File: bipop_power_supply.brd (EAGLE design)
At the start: 82.5 x 70.8 mm, 33 parts, among them IC1 LM1117MP-3.3, IC2 LM1117MP-5.0, X2 MSTBA6

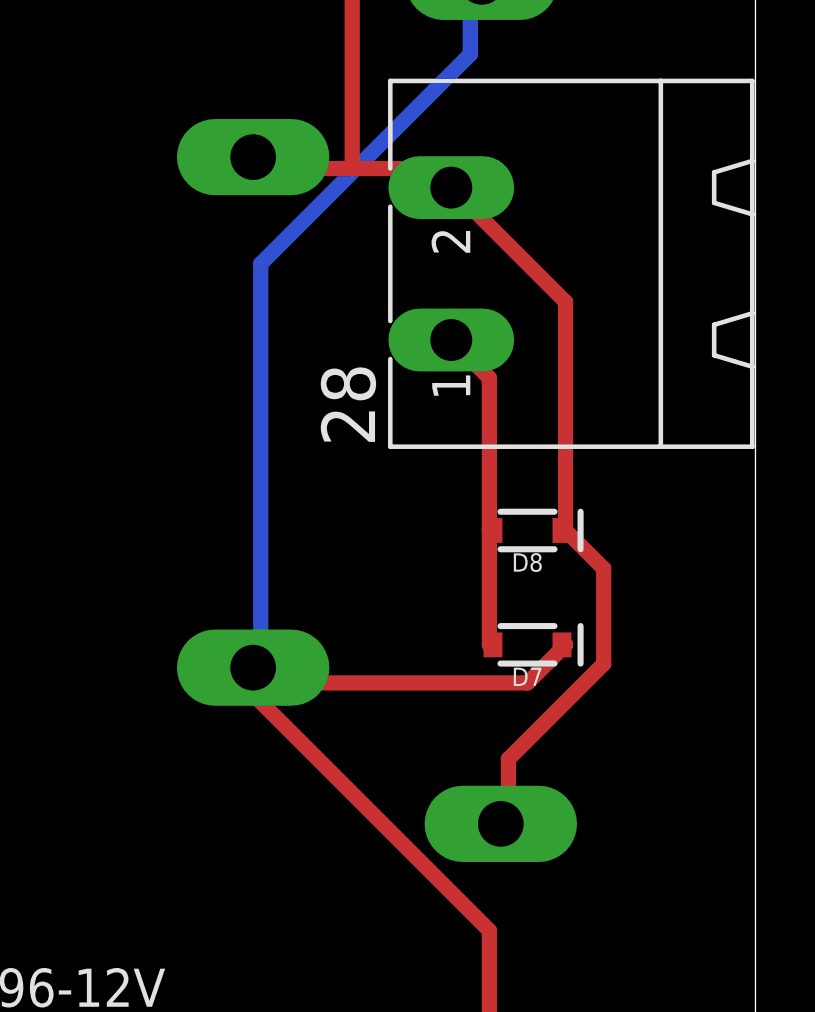
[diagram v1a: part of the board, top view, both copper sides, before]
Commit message: changed diodes' packages
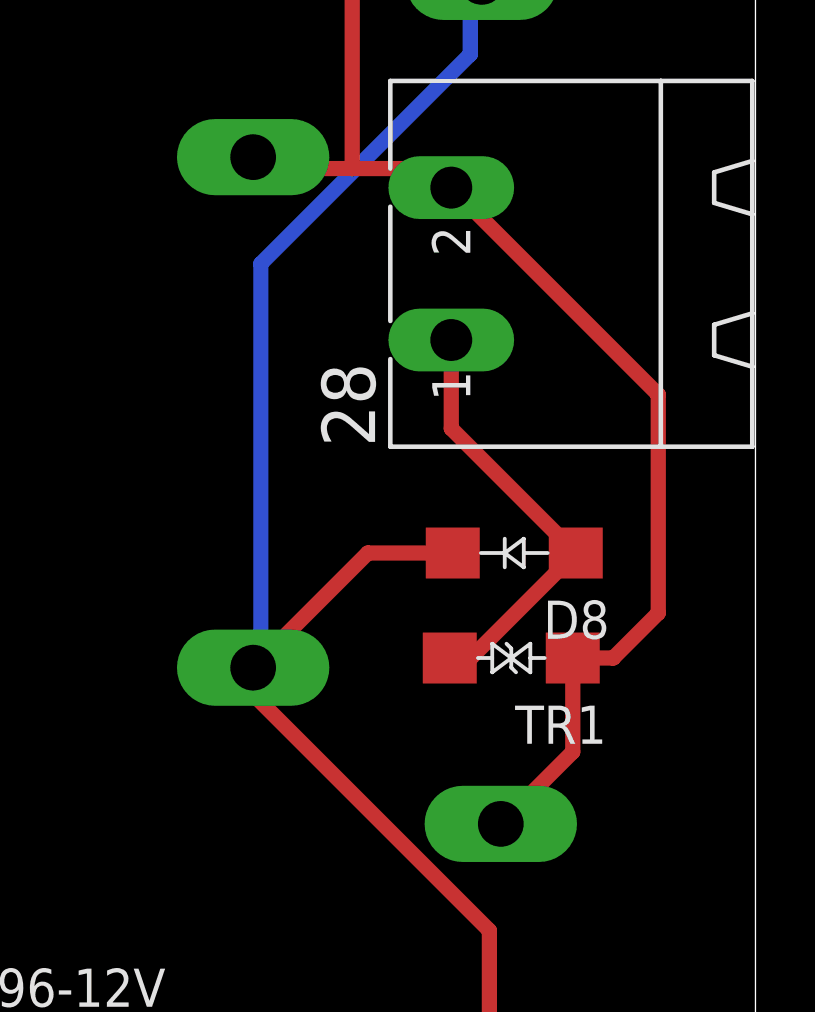
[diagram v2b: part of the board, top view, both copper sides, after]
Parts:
- removed D7: 20V, SparkFun-DiscreteSemi:SOD-323
- added TR1: SMBJ30CA-TR, transil:DO214AC_BIDIR
- D8: value 33.3V -> GF1; device SparkFun-DiscreteSemi:SOD-323 -> _mod_diode:SMA-DO214AC
- moved D8 0.87 mm to (78.3, 31.0)
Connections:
- net MM: now also D8.K; no longer D7.C
- net N$10: now also TR1.P$1; no longer D8.C
- net N$12: now also TR1.P$2; no longer D7.A
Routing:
- net N$12: track 10.9 -> 14.5 mm
- net MM: track 63.5 -> 60.3 mm
- net N$10: track 57.0 -> 59.1 mm
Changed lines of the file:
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@@
 <?xml version="1.0" encoding="utf-8"?>
 <!DOCTYPE eagle SYSTEM "eagle.dtd">
-<eagle version="8.5.1">
+<eagle version="8.3.2">
 <drawing>
 <settings>
@@
 <setting verticaltext="up"/>
 </settings>
-<grid distance="10" unitdist="mil" unit="mil" style="lines" multiple="1" display="yes" altdistance="5" altunitdist="mil" altunit="mil"/>
+<grid distance="0.1" unitdist="mm" unit="mm" style="lines" multiple="1" display="yes" altdistance="5" altunitdist="mil" altunit="mil"/>
 <layers>
 <layer number="1" name="Top" color="4" fill="1" visible="yes" active="yes"/>
@@
 <param name="dpMaxLengthDifference" value="10mm"/>
 <param name="dpGapFactor" value="2.5"/>
+<param name="checkGrid" value="0"/>
 <param name="checkAngle" value="0"/>
 <param name="checkFont" value="1"/>
 <param name="checkRestrict" value="1"/>
-<param name="checkStop" value="0"/>
-<param name="checkValues" value="0"/>
 <param name="useDiameter" value="13"/>
 <param name="maxErrors" value="50"/>
@@
 </element>
 <element name="U$4" library="frames" library_urn="urn:adsk.eagle:library:229" package="A5P-LOC" value="" x="-31.75" y="-48.26"/>
-<element name="D7" library="SparkFun-DiscreteSemi" package="SOD-323" value="20V" x="78.74" y="27.94" rot="R180">
-<attribute name="PROD_ID" value="DIO-11284" x="78.74" y="27.94" size="1.778" layer="27" rot="R180" display="off"/>
-</element>
 <element name="C1" library="rcl" library_urn="urn:adsk.eagle:library:334" package="C0805" package3d_urn="urn:adsk.eagle:package:23617/2" value="100uF" x="25.146" y="34.29" rot="R90"/>
-<element name="D8" library="SparkFun-DiscreteSemi" package="SOD-323" value="33.3V" x="78.74" y="31.75" rot="R180">
-<attribute name="PROD_ID" value="DIO-11284" x="78.74" y="31.75" size="1.778" layer="27" rot="R180" display="off"/>
-</element>
 <element name="C2" library="rcl" library_urn="urn:adsk.eagle:library:334" package="C0805" package3d_urn="urn:adsk.eagle:package:23617/2" value="100uF" x="25.146" y="40.64" rot="R90"/>
 <element name="C3" library="rcl" library_urn="urn:adsk.eagle:library:334" package="C0805" package3d_urn="urn:adsk.eagle:package:23617/2" value="100uF" x="25.146" y="46.736" rot="R90"/>
@@
 <element name="R2" library="rcl" library_urn="urn:adsk.eagle:library:334" package="R0805" package3d_urn="urn:adsk.eagle:package:23553/2" value="4.7k" x="12.573" y="9.525" rot="R270"/>
 <element name="R3" library="rcl" library_urn="urn:adsk.eagle:library:334" package="R0805" package3d_urn="urn:adsk.eagle:package:23553/2" value="4.7k" x="6.985" y="26.035" rot="R270"/>
+<element name="TR1" library="transil" package="DO214AC_BIDIR" value="SMBJ30CA-TR" x="78.2" y="27.5" rot="R180"/>
+<element name="D8" library="_mod_diode" package="SMA-DO214AC" value="GF1" x="78.3" y="31" rot="R180"/>
 </elements>
 <signals>
@@
 </signal>
 <signal name="N$10">
-<contactref element="D8" pad="C"/>
 <contactref element="U$1" pad="V_IN-"/>
 <contactref element="U$2" pad="V_IN-"/>
 <contactref element="U$3" pad="V_IN-"/>
 <contactref element="28" pad="2"/>
-<wire x1="80.01" y1="39.37" x2="80.01" y2="31.75" width="0.508" layer="1"/>
-<wire x1="76.2" y1="43.18" x2="80.01" y2="39.37" width="0.508" layer="1"/>
-<wire x1="78.105" y1="24.13" x2="78.105" y2="22.225" width="0.508" layer="1"/>
-<wire x1="81.28" y1="27.305" x2="78.105" y2="24.13" width="0.508" layer="1"/>
-<wire x1="81.28" y1="30.48" x2="81.28" y2="27.305" width="0.508" layer="1"/>
-<wire x1="80.01" y1="31.75" x2="81.28" y2="30.48" width="0.508" layer="1"/>
-<wire x1="78.105" y1="22.225" x2="77.851" y2="21.971" width="0.508" layer="1"/>
-<wire x1="80.01" y1="31.75" x2="79.89" y2="31.75" width="0.508" layer="1"/>
 <wire x1="75.565" y1="43.815" x2="72.898" y2="43.815" width="0.508" layer="1"/>
 <wire x1="72.898" y1="43.815" x2="69.85" y2="43.815" width="0.508" layer="1"/>
@@
 <wire x1="72.898" y1="43.815" x2="72.898" y2="53.086" width="0.508" layer="1"/>
 <wire x1="76.835" y1="66.675" x2="77.216" y2="67.056" width="0.508" layer="1"/>
+<contactref element="TR1" pad="P$1"/>
+<wire x1="77.851" y1="21.971" x2="80.25" y2="24.37" width="0.508" layer="1"/>
+<wire x1="80.25" y1="24.37" x2="80.25" y2="27.5" width="0.508" layer="1"/>
+<wire x1="80.25" y1="27.5" x2="81.6" y2="27.5" width="0.508" layer="1"/>
+<wire x1="81.6" y1="27.5" x2="83.1" y2="29" width="0.508" layer="1"/>
+<wire x1="83.1" y1="29" x2="83.1" y2="36.28" width="0.508" layer="1"/>
+<wire x1="83.1" y1="36.28" x2="76.2" y2="43.18" width="0.508" layer="1"/>
 </signal>
 <signal name="N$12">
+<contactref element="28" pad="1"/>
+<contactref element="TR1" pad="P$2"/>
 <contactref element="D8" pad="A"/>
-<contactref element="D7" pad="A"/>
-<contactref element="28" pad="1"/>
-<wire x1="77.47" y1="31.75" x2="77.47" y2="27.94" width="0.508" layer="1"/>
-<wire x1="77.47" y1="27.94" x2="77.59" y2="27.94" width="0.508" layer="1"/>
-<wire x1="77.47" y1="36.83" x2="77.47" y2="31.75" width="0.508" layer="1"/>
-<wire x1="76.2" y1="38.1" x2="77.47" y2="36.83" width="0.508" layer="1"/>
-<wire x1="77.47" y1="31.75" x2="77.59" y2="31.75" width="0.508" layer="1"/>
+<wire x1="76.85" y1="27.5" x2="80.35" y2="31" width="0.508" layer="1"/>
+<wire x1="76.85" y1="27.5" x2="76.15" y2="27.5" width="0.508" layer="1"/>
+<wire x1="80.35" y1="31" x2="76.2" y2="35.15" width="0.508" layer="1"/>
+<wire x1="76.2" y1="35.15" x2="76.2" y2="38.1" width="0.508" layer="1"/>
 </signal>
 <signal name="VIOUT_5">
@@
 <signal name="MM">
 <contactref element="U$1" pad="V_IN+"/>
-<contactref element="D7" pad="C"/>
 <contactref element="U$2" pad="V_IN+"/>
 <contactref element="U$3" pad="V_IN+"/>
-<wire x1="78.74" y1="26.67" x2="80.01" y2="27.94" width="0.508" layer="1"/>
-<wire x1="69.85" y1="26.67" x2="78.74" y2="26.67" width="0.508" layer="1"/>
-<wire x1="80.01" y1="27.94" x2="79.89" y2="27.94" width="0.508" layer="1"/>
-<wire x1="69.85" y1="26.67" x2="69.596" y2="27.178" width="0.508" layer="1"/>
 <wire x1="77.47" y1="18.415" x2="77.47" y2="5.08" width="0.508" layer="1"/>
 <wire x1="69.215" y1="26.67" x2="77.47" y2="18.415" width="0.508" layer="1"/>
 <wire x1="77.47" y1="5.08" x2="77.851" y2="4.953" width="0.508" layer="1"/>
-<wire x1="69.215" y1="26.67" x2="69.596" y2="27.178" width="0.508" layer="1"/>
+<wire x1="69.596" y1="27.178" x2="69.215" y2="26.67" width="0.508" layer="1"/>
 <wire x1="76.835" y1="47.625" x2="76.835" y2="49.53" width="0.508" layer="16"/>
 <wire x1="69.85" y1="40.64" x2="76.835" y2="47.625" width="0.508" layer="16"/>
@@
 <wire x1="76.835" y1="49.53" x2="77.216" y2="50.038" width="0.508" layer="16"/>
 <wire x1="69.85" y1="27.305" x2="69.596" y2="27.178" width="0.508" layer="16"/>
+<contactref element="D8" pad="K"/>
+<wire x1="76.25" y1="31" x2="73.418" y2="31" width="0.508" layer="1"/>
+<wire x1="73.418" y1="31" x2="69.596" y2="27.178" width="0.508" layer="1"/>
 </signal>
 <signal name="N$1">

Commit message: small board adjustments, ready to gerber
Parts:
- moved U$1 0.50 mm to (58.6, 13.3)
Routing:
- net 12_IN: track 18.8 -> 18.0 mm
- net MM: track 60.3 -> 59.7 mm
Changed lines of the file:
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@@
 <setting verticaltext="up"/>
 </settings>
-<grid distance="0.1" unitdist="mm" unit="mm" style="lines" multiple="1" display="yes" altdistance="5" altunitdist="mil" altunit="mil"/>
+<grid distance="0.5" unitdist="mm" unit="mm" style="lines" multiple="1" display="yes" altdistance="5" altunitdist="mil" altunit="mil"/>
 <layers>
 <layer number="1" name="Top" color="4" fill="1" visible="yes" active="yes"/>
@@
 <dimension x1="3.81" y1="0" x2="3.81" y2="70.79" x3="0" y3="35.395" textsize="1.778" layer="20" precision="1"/>
 <dimension x1="3.81" y1="70.79" x2="86.34" y2="70.79" x3="45.075" y3="73.66" textsize="1.778" layer="20" precision="1"/>
-<hole x="6.985" y="3.175" drill="3.39999375"/>
-<hole x="6.985" y="67.945" drill="3.39999375"/>
-<hole x="83.185" y="67.945" drill="3.39999375"/>
-<hole x="83.185" y="3.175" drill="3.39999375"/>
+<hole x="7" y="68" drill="3.4"/>
+<hole x="7" y="3" drill="3.4"/>
+<hole x="83" y="68" drill="3.4"/>
+<hole x="83" y="3" drill="3.4"/>
 </plain>
 <attributes>
@@
 <attribute name="PROD_ID" value="DIO-11623" x="21.59" y="67.31" size="1.778" layer="27" display="off"/>
 </element>
-<element name="U$1" library="lustro_pcb" package="DC-DC_CONVERTER" value="LM2596-12V" x="59.055" y="13.335" rot="R180"/>
+<element name="U$1" library="lustro_pcb" package="DC-DC_CONVERTER" value="LM2596-12V" x="58.555" y="13.335" rot="R180"/>
 <element name="U$2" library="lustro_pcb" package="DC-DC_CONVERTER" value="LM2596-5V" x="50.8" y="35.56" rot="R180"/>
 <element name="U$3" library="lustro_pcb" package="DC-DC_CONVERTER" value="LM2596-3V3" x="58.42" y="58.42" rot="R180"/>
@@
 <wire x1="32.385" y1="21.59" x2="32.145" y2="21.95" width="0.508" layer="1"/>
 <wire x1="32.385" y1="22.225" x2="38.1" y2="22.225" width="0.508" layer="1"/>
-<wire x1="38.1" y1="22.225" x2="38.481" y2="21.971" width="0.508" layer="1"/>
+<wire x1="38.1" y1="22.225" x2="37.981" y2="21.971" width="0.508" layer="1"/>
 <wire x1="32.385" y1="22.225" x2="32.145" y2="21.95" width="0.508" layer="1"/>
 <wire x1="22.86" y1="22.86" x2="22.86" y2="18.415" width="0.508" layer="1"/>
@@
 <wire x1="76.835" y1="66.675" x2="77.216" y2="67.056" width="0.508" layer="1"/>
 <contactref element="TR1" pad="P$1"/>
-<wire x1="77.851" y1="21.971" x2="80.25" y2="24.37" width="0.508" layer="1"/>
+<wire x1="77.351" y1="21.971" x2="80.25" y2="24.37" width="0.508" layer="1"/>
 <wire x1="80.25" y1="24.37" x2="80.25" y2="27.5" width="0.508" layer="1"/>
 <wire x1="80.25" y1="27.5" x2="81.6" y2="27.5" width="0.508" layer="1"/>
@@
 <wire x1="24.892" y1="3.175" x2="22.86" y2="3.175" width="0.508" layer="1"/>
 <wire x1="26.543" y1="2.54" x2="24.892" y2="3.175" width="0.508" layer="1"/>
-<wire x1="36.195" y1="2.54" x2="26.543" y2="2.54" width="0.508" layer="1"/>
-<wire x1="38.1" y1="4.445" x2="36.195" y2="2.54" width="0.508" layer="1"/>
+<wire x1="34.195" y1="2.54" x2="26.543" y2="2.54" width="0.508" layer="1"/>
+<wire x1="37.1" y1="4.445" x2="34.195" y2="2.54" width="0.508" layer="1"/>
 <wire x1="22.86" y1="3.175" x2="22.485" y2="3.17" width="0.508" layer="1"/>
-<wire x1="38.1" y1="4.445" x2="38.481" y2="4.953" width="0.508" layer="1"/>
+<wire x1="37.1" y1="4.445" x2="37.981" y2="4.953" width="0.508" layer="1"/>
 </signal>
 <signal name="3_OUT">
@@
 <wire x1="10.795" y1="33.655" x2="12.7" y2="31.75" width="0.508" layer="16"/>
 <wire x1="10.795" y1="60.325" x2="10.795" y2="33.655" width="0.508" layer="16"/>
-<wire x1="13.335" y1="62.865" x2="10.795" y2="60.325" width="0.508" layer="16"/>
-<wire x1="21.59" y1="62.865" x2="13.335" y2="62.865" width="0.508" layer="16"/>
-<wire x1="22.86" y1="64.135" x2="21.59" y2="62.865" width="0.508" layer="1"/>
+<wire x1="13.035" y1="62.565" x2="10.795" y2="60.325" width="0.508" layer="16"/>
+<wire x1="21.59" y1="62.565" x2="13.035" y2="62.565" width="0.508" layer="16"/>
+<wire x1="22.86" y1="64.135" x2="21.59" y2="62.565" width="0.508" layer="1"/>
 <wire x1="16.51" y1="27.94" x2="16.77" y2="27.935" width="0.508" layer="1"/>
 <wire x1="22.86" y1="64.135" x2="22.74" y2="64.135" width="0.508" layer="1"/>
 <via x="12.7" y="31.75" extent="1-16" drill="0.35"/>
-<via x="21.59" y="62.865" extent="1-16" drill="0.35"/>
+<via x="21.59" y="62.565" extent="1-16" drill="0.35"/>
 </signal>
 <signal name="VIOUT_3">
@@
 <contactref element="U$2" pad="V_IN+"/>
 <contactref element="U$3" pad="V_IN+"/>
-<wire x1="77.47" y1="18.415" x2="77.47" y2="5.08" width="0.508" layer="1"/>
-<wire x1="69.215" y1="26.67" x2="77.47" y2="18.415" width="0.508" layer="1"/>
-<wire x1="77.47" y1="5.08" x2="77.851" y2="4.953" width="0.508" layer="1"/>
-<wire x1="69.596" y1="27.178" x2="69.215" y2="26.67" width="0.508" layer="1"/>
+<wire x1="77.47" y1="15.715" x2="77.47" y2="5.08" width="0.508" layer="1"/>
+<wire x1="69.615" y1="23.87" x2="77.47" y2="15.715" width="0.508" layer="1"/>
+<wire x1="77.47" y1="5.08" x2="77.351" y2="4.953" width="0.508" layer="1"/>
+<wire x1="69.596" y1="27.178" x2="69.615" y2="23.87" width="0.508" layer="1"/>
 <wire x1="76.835" y1="47.625" x2="76.835" y2="49.53" width="0.508" layer="16"/>
 <wire x1="69.85" y1="40.64" x2="76.835" y2="47.625" width="0.508" layer="16"/>
